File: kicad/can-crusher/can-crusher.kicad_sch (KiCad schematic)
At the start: 21 parts, among them J1 Stepper Left, J2 Control UART, J3 Ext power, J4 Stepper Right, J5 Barrel_Jack, J6 Expansion Port, Q1 IRF4905, Q2 BS170, SW1 Reboot, SW2 User Interaction, U1 BTT_TMC2209, U2 Pico, U3 BTT_TMC2209

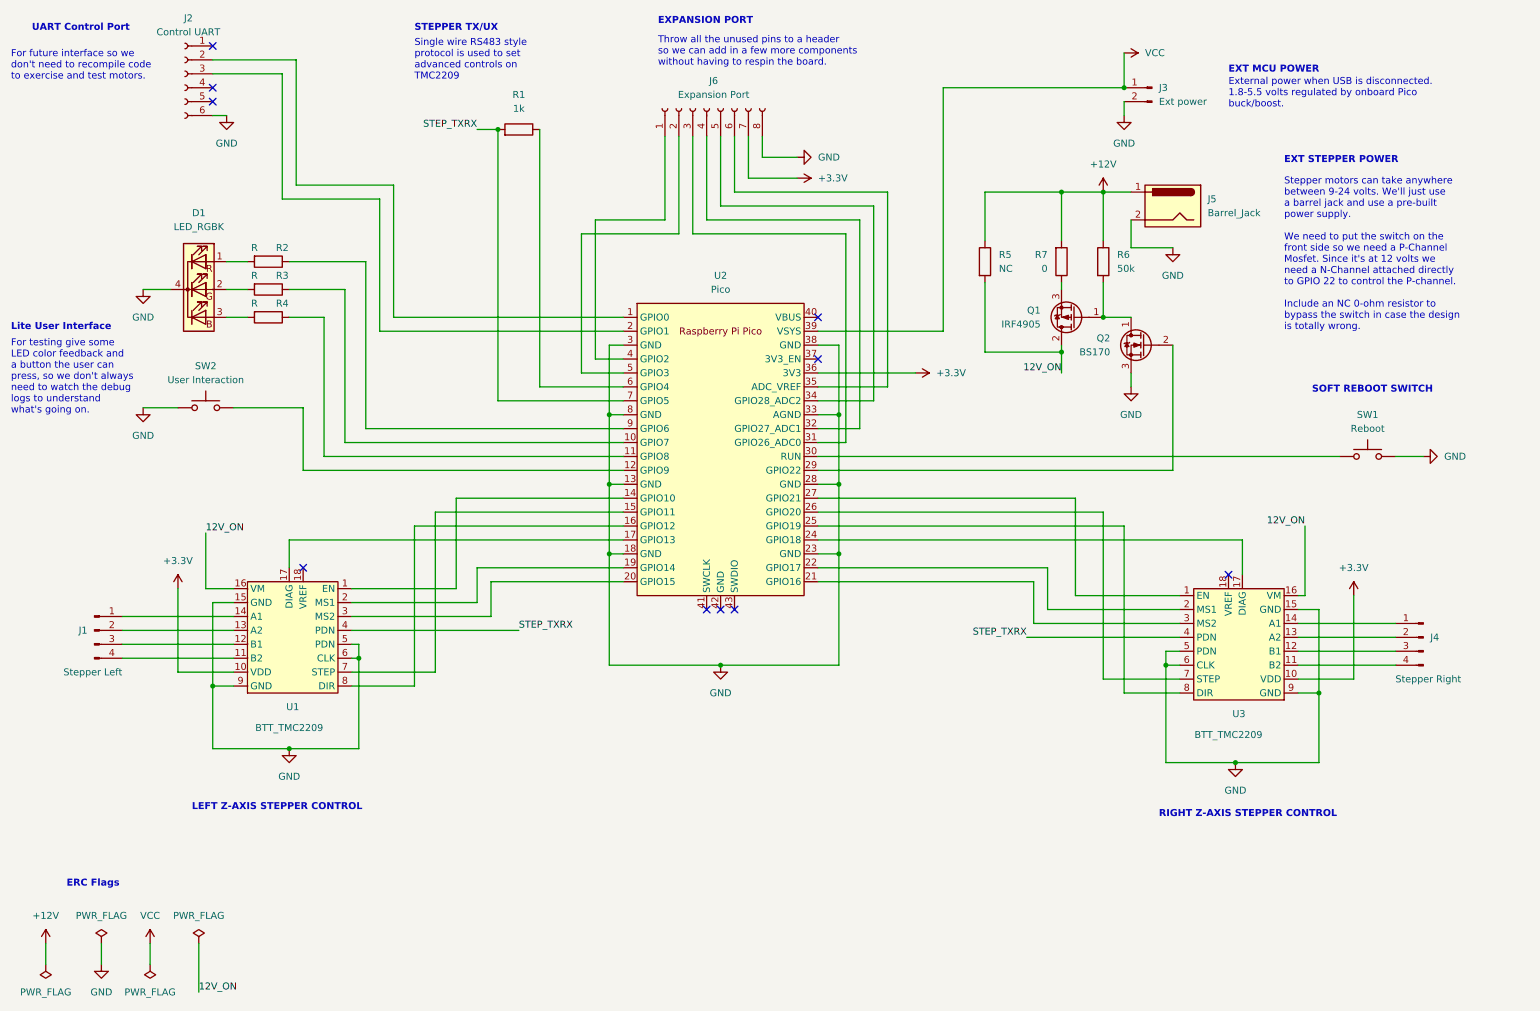
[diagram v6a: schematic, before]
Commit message: Rough out initial rats nest; Change pin assignments to make layout easier.
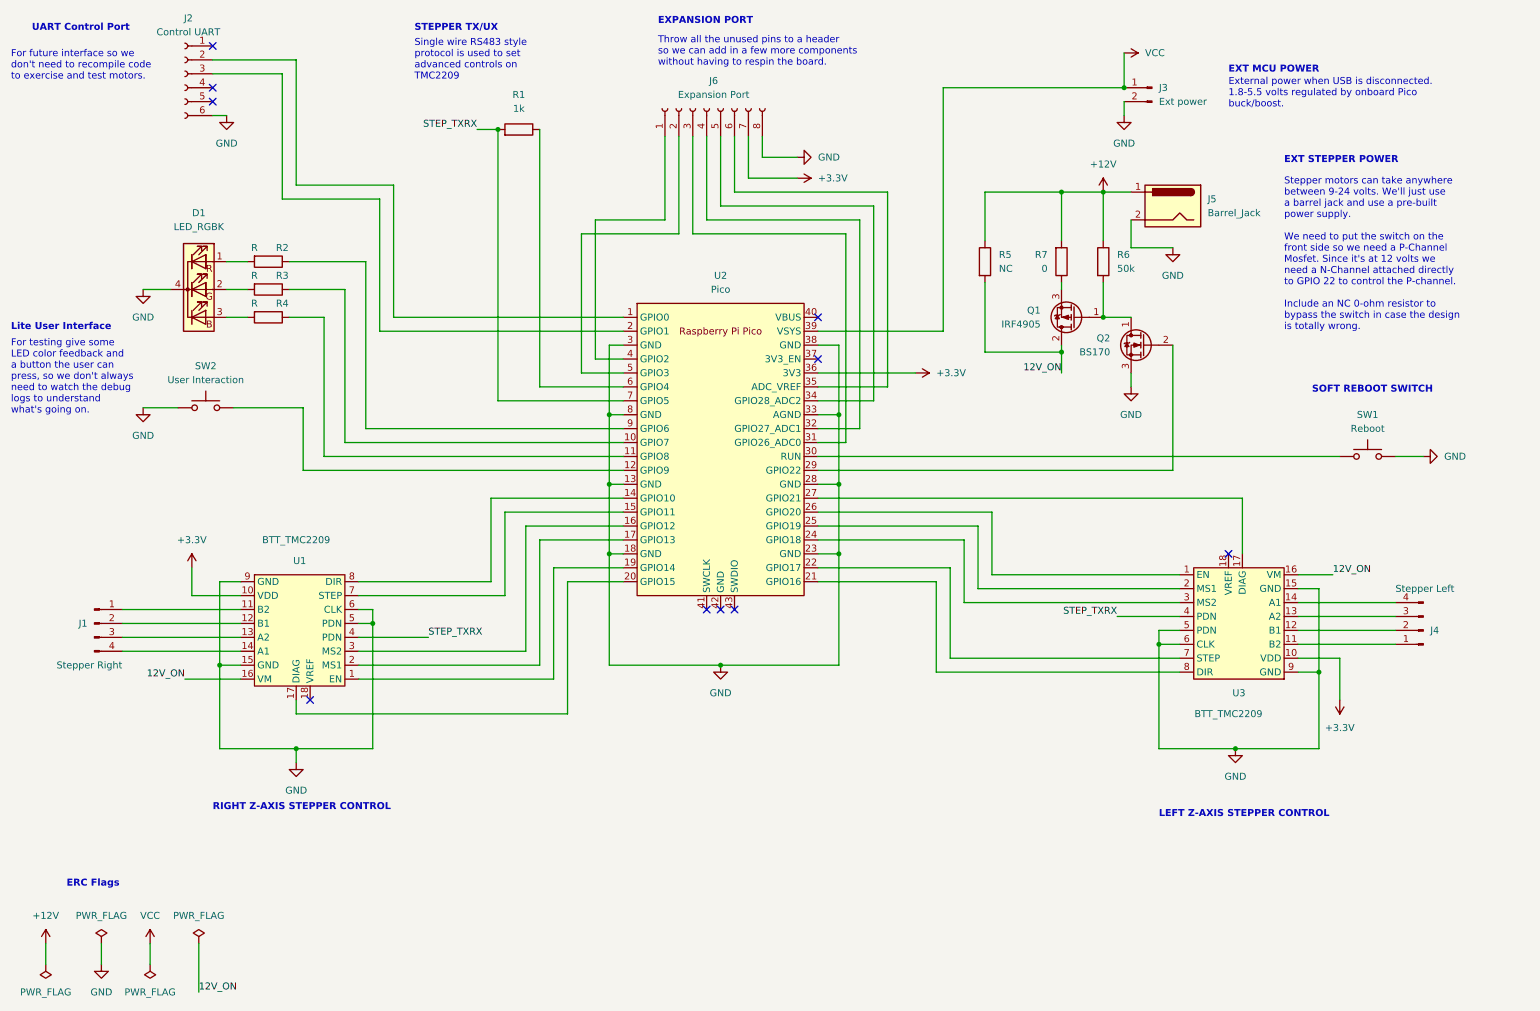
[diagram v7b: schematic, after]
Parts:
- J1: value Stepper Left -> Stepper Right
- J4: value Stepper Right -> Stepper Left
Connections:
- net at J1.1 (Pin_1): now also U1.11 (B2); no longer U1.14 (A1)
- net at J1.2 (Pin_2): now also U1.12 (B1); no longer U1.13 (A2)
- net at J1.3 (Pin_3): now also U1.13 (A2); no longer U1.12 (B1)
- net at J1.4 (Pin_4): now also U1.14 (A1); no longer U1.11 (B2)
- net at U1.1 (EN): now also U2.19 (GPIO14); no longer U2.14 (GPIO10)
- net at U1.17 (DIAG): now also U2.20 (GPIO15); no longer U2.17 (GPIO13)
- net at U1.2 (MS1): now also U2.17 (GPIO13); no longer U2.19 (GPIO14)
- net at U1.3 (MS2): now also U2.16 (GPIO12); no longer U2.20 (GPIO15)
- net at U1.8 (DIR): now also U2.14 (GPIO10); no longer U2.16 (GPIO12)
- net at U3.1 (EN): now also U2.26 (GPIO20); no longer U2.27 (GPIO21)
- net at U3.11 (B2): now also J4.1 (Pin_1); no longer J4.4 (Pin_4)
- net at U3.12 (B1): now also J4.2 (Pin_2); no longer J4.3 (Pin_3)
- net at U3.13 (A2): now also J4.3 (Pin_3); no longer J4.2 (Pin_2)
- net at U3.14 (A1): now also J4.4 (Pin_4); no longer J4.1 (Pin_1)
- net at U3.17 (DIAG): now also U2.27 (GPIO21); no longer U2.24 (GPIO18)
- net at U3.2 (MS1): now also U2.25 (GPIO19); no longer U2.22 (GPIO17)
- net at U3.3 (MS2): now also U2.24 (GPIO18); no longer U2.21 (GPIO16)
- net at U3.7 (STEP): now also U2.22 (GPIO17); no longer U2.26 (GPIO20)
- net at U3.8 (DIR): now also U2.21 (GPIO16); no longer U2.25 (GPIO19)
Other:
- moved on the sheet: J1, J4, U1, U3

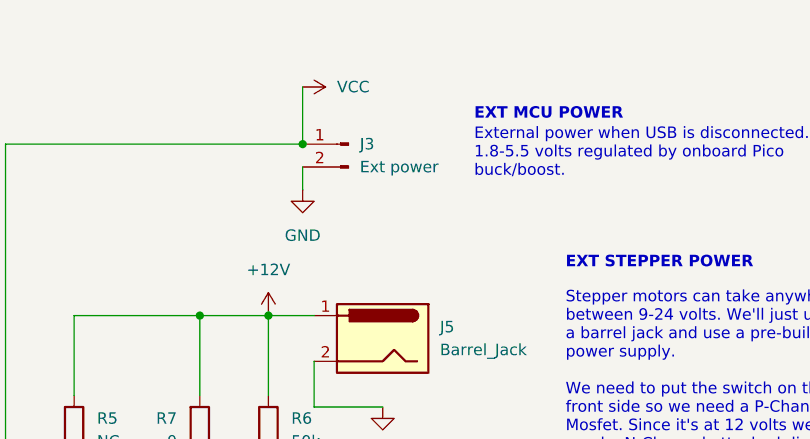
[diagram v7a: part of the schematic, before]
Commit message: Give better name to project lib storage dir
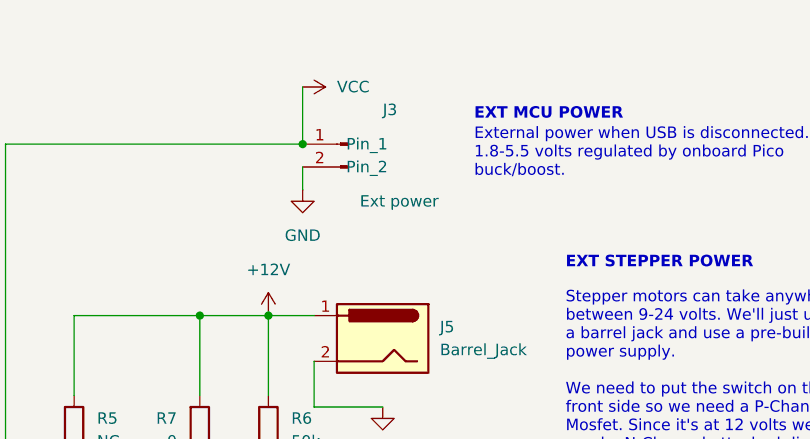
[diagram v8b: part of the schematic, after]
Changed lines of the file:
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@@
   )
   (symbol (lib_id "Connector:Conn_01x02_Male") (at 223.52 27.94 0) (mirror y) (unit 1)
-    (in_bom yes) (on_board yes) (fields_autoplaced)
-    (property "Reference" "J3" (id 0) (at 224.79 27.9399 0)
+    (in_bom yes) (on_board yes)
+    (property "Reference" "J3" (id 0) (at 227.33 24.13 0)
       (effects (font (size 1.27 1.27)) (justify right))
     )
-    (property "Value" "Ext power" (id 1) (at 224.79 30.4799 0)
+    (property "Value" "Ext power" (id 1) (at 224.79 34.29 0)
       (effects (font (size 1.27 1.27)) (justify right))
     )
